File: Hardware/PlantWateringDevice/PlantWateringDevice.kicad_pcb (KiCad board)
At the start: 4 copper layers, 50 x 50 mm, 87 parts, among them J1 Conn_01x03_Pin, J3 Conn_01x03_Pin, J5 Conn_02x03_Odd_Even, J6 Barrel_Jack_Switch, M1 Motor_DC, Q1 AO3404A, SW1 SW_Push, SW6 SW_Push, SW7 SW_DIP_x02, SW8 SW_Push, U1 MCP6002-xSN, U10 74HC595, U2 L78L33_SO8, U3 PIC10F200-IOT, U4 74LVC1G3157, U5 74HC595, U9 74HC4052D

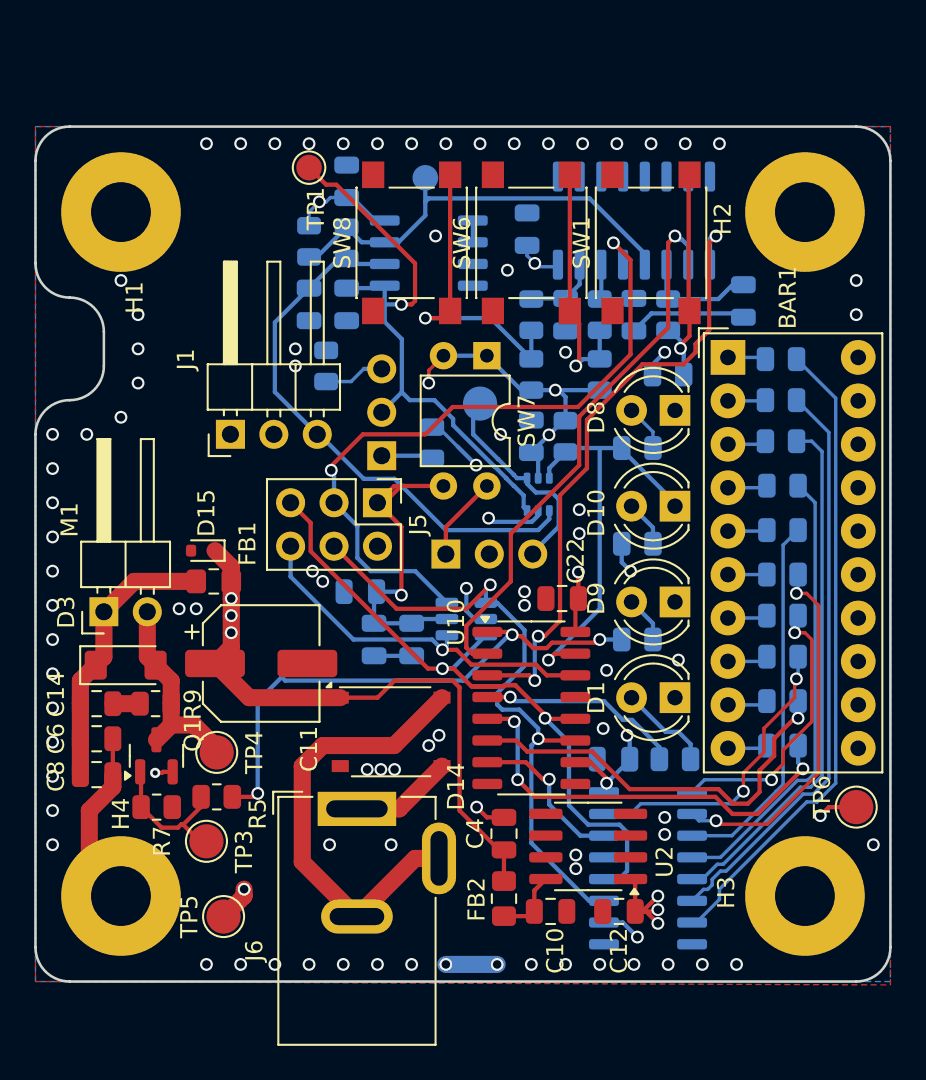
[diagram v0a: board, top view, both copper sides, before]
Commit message: circuit simplification
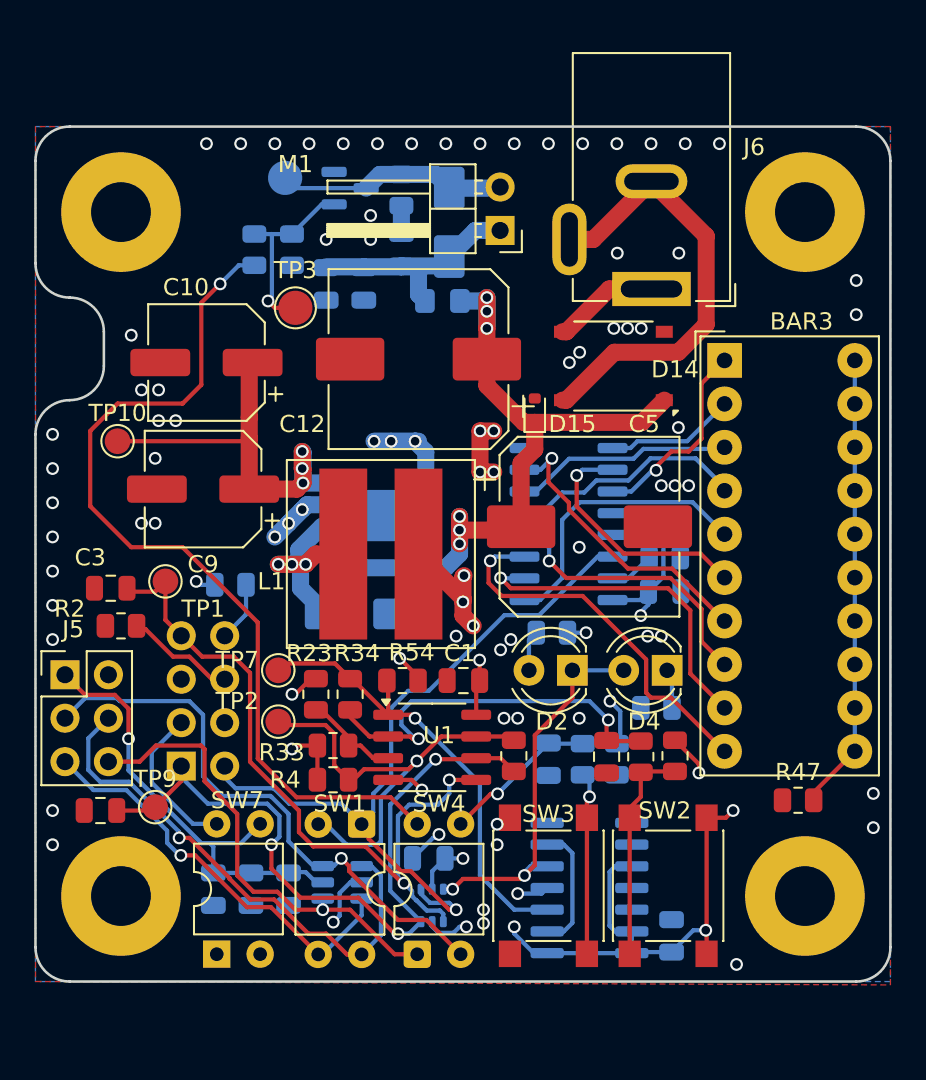
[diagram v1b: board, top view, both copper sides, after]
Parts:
- removed BAR1: HDSP-4830_2, Display:HDSP-4830
- removed C11: 100u/12v, Capacitor_SMD:CP_Elec_6.3x5.8
- removed C20, C22, C23, C24: 100n, Capacitor_SMD:C_0805_2012Metric
- removed D10, D8, D9: LED, LED_THT:LED_D4.0mm
- removed D3: D, Diode_SMD:D_MiniMELF
- removed FB2: FerriteBead, Inductor_SMD:L_0805_2012Metric_Pad1.15x1.40mm_HandSolder
- removed J3: Conn_01x03_Pin, Connector_PinHeader_2.54mm:PinHeader_1x03_P2.54mm_Vertical
- removed R10, R12, R13, R14, R15, R16, R17, R18, R19, R20, R21, R22: 220R, Resistor_SMD:R_0805_2012Metric
- removed R25, R27, R29: 10k, Resistor_SMD:R_0805_2012Metric
- removed R26, R28, R30: 100R, Resistor_SMD:R_0805_2012Metric
- removed RV1: 100k, Connector_PinHeader_2.54mm:PinHeader_1x03_P2.54mm_Vertical
- removed SW6, SW8: SW_Push, Button_Switch_SMD:SW_SPST_PTS645
- removed TP5, TP6, TP8: TestPoint, TestPoint:TestPoint_Pad_D2.0mm
- removed U10: 74HC595, Package_SO:SO-16_3.9x9.9mm_P1.27mm
- removed U4: 74LVC1G3157, Package_TO_SOT_SMD:SOT-363_SC-70-6
- removed U9: 74HC4052D, Package_SO:SO-16_3.9x9.9mm_P1.27mm
- added BAR3: HDSP-4830_2, Display:HDSP-4830, F.Cu at (175.3, 53.7)
- added C17: 100n, Capacitor_SMD:C_0805_2012Metric, B.Cu at (172.2, 87.3)
- added C21: 100n, Capacitor_SMD:C_0805_2012Metric, B.Cu at (171.8, 67.2)
- added C25: 100n, Capacitor_SMD:C_0805_2012Metric, B.Cu at (171.8, 63.2)
- added C7: 100n, Capacitor_SMD:C_0805_2012Metric, F.Cu at (168.4, 76.8)
- added D2: LED, LED_THT:LED_D4.0mm, F.Cu at (166.4, 71.8)
- added D4: LED, LED_THT:LED_D4.0mm, F.Cu at (171.9, 71.8)
- added D5: D_Schottky, Diode_SMD:D_SMA, B.Cu at (154.0, 68.5)
- added L1: 33u, PlantWateringDevice:SDR1006-330KL, F.Cu at (155.2, 65.0)
- added R11: 10k, Resistor_SMD:R_0805_2012Metric, F.Cu at (172.4, 76.8)
- added R24: 10k, Resistor_SMD:R_0805_2012Metric, F.Cu at (170.4, 76.8)
- added R31: 220R, Resistor_SMD:R_0805_2012Metric, B.Cu at (165.2, 69.6)
- added R32: 220R, Resistor_SMD:R_0805_2012Metric, B.Cu at (171.3, 74.0)
- added R33: 10k, Resistor_SMD:R_0805_2012Metric, F.Cu at (152.4, 76.2)
- added R34: 100k, Resistor_SMD:R_0805_2012Metric, F.Cu at (153.4, 73.2)
- added R47: 220R, Resistor_SMD:R_0805_2012Metric, F.Cu at (179.6, 79.4)
- added R53: 22k, Resistor_SMD:R_0805_2012Metric, B.Cu at (171.8, 65.2)
- added R54: 1k, Resistor_SMD:R_0805_2012Metric, F.Cu at (156.5, 72.4)
- added SW2: SW_Push, Button_Switch_SMD:SW_SPST_PTS645, F.Cu at (172.0, 84.4)
- added SW3: SW_Push, Button_Switch_SMD:SW_SPST_PTS645, F.Cu at (165.0, 84.4)
- added SW4: SW_DIP_x02, Package_DIP:DIP-4_W7.62mm, F.Cu at (157.3, 88.4)
- added TP10: TestPoint, TestPoint:TestPoint_Pad_D1.5mm, F.Cu at (139.8, 58.4)
- added TP7: TestPoint, TestPoint:TestPoint_Pad_D1.5mm, F.Cu at (149.2, 71.8)
- added TP9: TestPoint, TestPoint:TestPoint_Pad_D1.5mm, F.Cu at (142.0, 79.8)
- added U6: 74HC74, Package_SO:SO-14_3.9x8.65mm_P1.27mm, B.Cu at (167.4, 84.5)
- added U7: 4017, Package_SO:SO-16_3.9x9.9mm_P1.27mm, B.Cu at (166.2, 63.2)
- C1, C2, C3, R2, R3, R4, TP2, U1: moved to F.Cu
- C10: value 1u -> 220u; footprint Capacitor_SMD:C_0805_2012Metric -> Capacitor_SMD:CP_Elec_6.3x5.8
- C12: value 1u -> 680u/12v; footprint Capacitor_SMD:C_0805_2012Metric -> Capacitor_SMD:CP_Elec_10x10
- C14, C6, C8, FB1, Q1, R5, R7, R9, TP4: moved to B.Cu
- C4: value 1u -> 100n; moved to B.Cu
- C5: value 100n -> 680u/12v; footprint Capacitor_SMD:C_0805_2012Metric -> Capacitor_SMD:CP_Elec_10x10; moved to F.Cu
- C9: value 100n -> 220u; footprint Capacitor_SMD:C_0805_2012Metric -> Capacitor_SMD:CP_Elec_6.3x5.8; moved to F.Cu
- D1: value LED -> D_Schottky; footprint LED_THT:LED_D4.0mm -> Diode_SMD:D_SMA; moved to B.Cu
- J1: value Conn_01x03_Pin -> Conn_02x04_Counter_Clockwise; footprint Connector_PinHeader_2.54mm:PinHeader_1x03_P2.54mm_Horizontal -> Connector_PinHeader_2.54mm:PinHeader_2x04_P2.54mm_Vertical; moved to B.Cu
- R23: value 100k -> 10k; moved to F.Cu
- R6, R8: value 220R -> 10k
- SW1: value SW_Push -> SW_DIP_x02; footprint Button_Switch_SMD:SW_SPST_PTS645 -> Package_DIP:DIP-4_W7.62mm
- U2: value L78L33_SO8 -> 74LVC1G3157; footprint Package_SO:SOIC-8_3.9x4.9mm_P1.27mm -> Package_TO_SOT_SMD:SOT-363_SC-70-6; moved to B.Cu
- U5: value 74HC595 -> LM2596S-3.3; footprint Package_SO:SO-16_3.9x9.9mm_P1.27mm -> Package_SO:Infineon_PG-DSO-8-27_3.9x4.9mm_EP2.65x3mm
- moved SW7 38.4 mm to (145.6, 88.4), turned to 90 degrees
- moved SW1 38.0 mm to (154.1, 80.8), turned to -90 degrees
- moved C10 37.9 mm to (145.0, 53.8), turned to 180 degrees
- moved Q1 35.1 mm to (153.4, 43.6), turned to 0 degrees
- moved J6 34.9 mm to (171.0, 49.5), turned to 180 degrees
- moved C12 34.4 mm to (157.4, 53.6)
- moved TP4 33.8 mm to (149.6, 43.0), turned to 180 degrees
- moved R7 33.5 mm to (150.0, 47.2), turned to -90 degrees
- moved R9 33.3 mm to (156.4, 43.7), turned to 90 degrees
- moved TP2 32.9 mm to (149.2, 74.8), turned to 0 degrees
- moved C8 32.7 mm to (154.2, 49.2), turned to -90 degrees
- moved M1 32.2 mm to (162.2, 46.1), turned to 180 degrees
- moved R5 32.1 mm to (147.8, 47.2), turned to 90 degrees
- moved C2 32.0 mm to (138.8, 80.0), turned to 180 degrees
- moved C14 32.0 mm to (156.4, 47.2), turned to 90 degrees
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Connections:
- net DATA_IN renamed Net-(J5-Pin_3)
- net DATA_OUT renamed Net-(J5-Pin_6)
- C10 pad 1: Net-(U2-IN) -> +3V3
- C12 pad 1: +3V3 -> Net-(D14-+)
- C13 pad 1: +3V3 -> BUTTON
- C14 pad 1: Net-(D3-K) -> Net-(D1-K)
- C4 pad 1: +5V -> +3V3
- C5 pad 1: Net-(U9-X1) -> Net-(D14-+)
- C6 pad 1: Net-(D3-K) -> Net-(D1-K)
- C8 pad 1: Net-(D3-K) -> Net-(D1-K)
- C9 pad 1: Net-(U9-X2) -> +3V3
- D1 pad 1: GND -> Net-(D1-K)
- D14 pad 1: +5V -> Net-(D14-+)
- D15 pad 1: +5V -> Net-(D14-+)
- FB1 pad 1: +5V -> Net-(D14-+)
- FB1 pad 2: Net-(D3-K) -> Net-(D1-K)
- J1 pad 1: +3V3 -> HUMIDITY_SENSOR_IN
- J1 pad 2: GND -> DISPLAY_DATA
- J1 pad 3: HUMIDITY_SENSOR_IN -> DISPLAY_POWER
- J5 pad 4: CLK -> Net-(J5-Pin_4)
- J5 pad 5: STROBE -> Net-(J5-Pin_5)
- M1 pad 1: Net-(D3-K) -> Net-(D1-K)
- M1 pad 2: Net-(D3-A) -> Net-(D1-A)
- Q1 pad 3: Net-(D3-A) -> Net-(D1-A)
- R1 pad 1: Net-(R1-Pad1) -> POT_UP
- R2 pad 2: Net-(R2-Pad2) -> POT_DOWN
- R23 pad 1: /OutMUX/ENA_A_1 -> Net-(U1A-+)
- R23 pad 2: +3V3 -> GND
- R6 pad 1: Net-(D10-A) -> +3V3
- R6 pad 2: +3V3 -> Net-(R6-Pad2)
- R8 pad 1: Net-(BAR1-A-Pad10) -> Net-(R6-Pad2)
- R8 pad 2: Net-(U10-QF) -> BUTTON
- R9 pad 2: Net-(D3-A) -> Net-(D1-A)
- SW1 pad 1: GND -> DISPLAY_DATA
- SW1 pad 2: Net-(R29-Pad2) -> HUMIDITY_SENSOR_OUT
- TP4 pad 1: Net-(D3-A) -> Net-(D1-A)
- U1 pad 1: Net-(U1A--) -> Net-(U6A-C)
- U1 pad 3: GND -> Net-(U1A-+)
- U2 pad 1: +3V3 -> HUMIDITY_SENSOR_COMP
- U2 pad 3: GND -> HUMIDITY_SENSOR_IN
- U2 pad 4: unconnected-(U2-NC-Pad4) -> DISPLAY_DATA
- U2 pad 5: unconnected-(U2-NC-Pad5) -> +3V3
- U2 pad 6: GND -> Net-(D2-K)
- U3 pad 1: CLK -> Net-(J5-Pin_4)
- U3 pad 3: STROBE -> Net-(J5-Pin_5)
- U5 pad 1: Net-(U5-QB) -> Net-(D14-+)
- U5 pad 3: Net-(U5-QD) -> GND
- U5 pad 4: Net-(U5-QE) -> +3V3
- U5 pad 5: Net-(U5-QF) -> GND
- U5 pad 6: Net-(U5-QG) -> (no net)
- U5 pad 7: Net-(U5-QH) -> (no net)
- U5 pad 8: GND -> (no net)
- U5 pad 9: unconnected-(U5-QH&apos;-Pad9) -> (no net)
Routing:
- net DISPLAY_DATA: track 0.00 -> 43.1 mm, vias 0 -> 1
- net STROBE: track 42.5 -> 0.00 mm, vias 2 -> 0
- net Net-(D14-+): track 0.00 -> 42.1 mm, vias 0 -> 6
- net CLK: track 38.0 -> 0.00 mm, vias 2 -> 0
- net Net-(U5-QH): track 37.6 -> 0.00 mm
- net +5V: track 37.5 -> 0.00 mm, vias 4 -> 0
- net BUTTON_2: track 36.9 -> 0.00 mm, vias 3 -> 0
- net Net-(U5-QG): track 34.1 -> 0.00 mm
- net +3V3: track 53.1 -> 86.4 mm, vias 16 -> 18
- net BUTTON_1: track 32.6 -> 0.00 mm, vias 1 -> 0
- net Net-(U5-QF): track 30.8 -> 0.00 mm
- net Net-(J5-Pin_4): track 0.00 -> 30.6 mm, vias 0 -> 1
- net Net-(U5-QE): track 26.5 -> 0.00 mm
- net Net-(BAR3-K-Pad11): track 0.00 -> 26.3 mm
- net Net-(U6A-C): track 0.00 -> 25.7 mm, vias 0 -> 1
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- added copper zone on In1.Cu, net Net-(D14-+)
- removed copper zone on In1.Cu, net +5V

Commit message: model of 3d printed holder
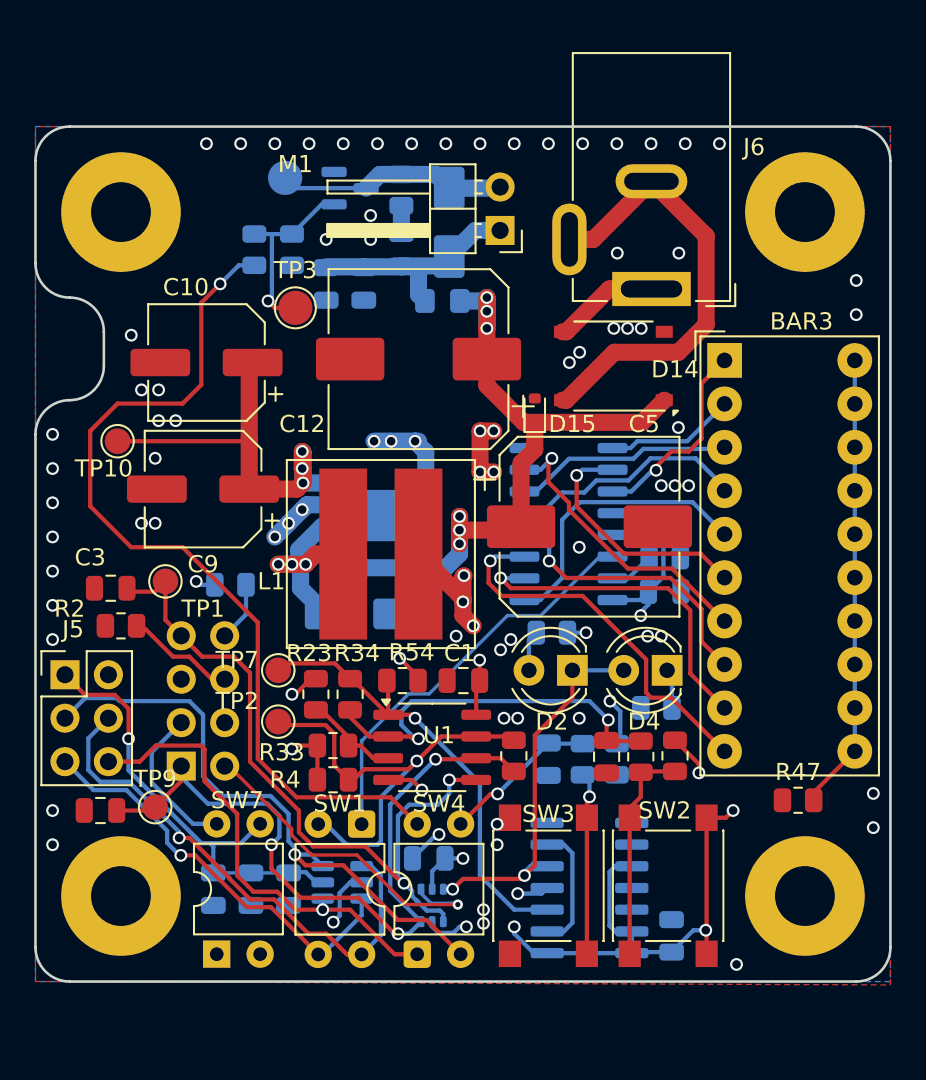
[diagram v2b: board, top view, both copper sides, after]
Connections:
- SW1 pad 1: DISPLAY_DATA -> DISPLAY_BARGRAPH
- U7 pad 14: DISPLAY_DATA -> DISPLAY_BARGRAPH
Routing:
- net DISPLAY_DATA: track 43.1 -> 19.6 mm
- net DISPLAY_BARGRAPH: track 0.00 -> 23.3 mm
- net Net-(J5-Pin_3): track 32.9 -> 35.0 mm

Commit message: improvements after eric's comments
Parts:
- removed C10, C9: 220u, Capacitor_SMD:CP_Elec_6.3x5.8
- removed D1, D5: D_Schottky, Diode_SMD:D_SMA
- removed D15: ESD5Zxx, Diode_SMD:D_SOD-523
- removed FB1: FerriteBead, Inductor_SMD:L_0805_2012Metric_Pad1.15x1.40mm_HandSolder
- removed L1: 33u, PlantWateringDevice:SDR1006-330KL
- removed U5: LM2596S-3.3, Package_SO:Infineon_PG-DSO-8-27_3.9x4.9mm_EP2.65x3mm
- TP4: moved to F.Cu
- moved TP4 15.0 mm to (164.6, 43.0), turned to 0 degrees
- moved TP3 2.06 mm to (149.2, 52.4)
- moved TP10 1.00 mm to (139.0, 59.0)
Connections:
- C1 pad 1: +3V3 -> VCC
- C12 pad 1: Net-(D14-+) -> VCC
- C14 pad 1: Net-(D1-K) -> VCC
- C17 pad 1: +3V3 -> VCC
- C21 pad 1: +3V3 -> VCC
- C25 pad 1: +3V3 -> VCC
- C4 pad 1: +3V3 -> VCC
- C5 pad 1: Net-(D14-+) -> VCC
- C6 pad 1: Net-(D1-K) -> VCC
- C8 pad 1: Net-(D1-K) -> VCC
- D14 pad 1: Net-(D14-+) -> VCC
- J1 pad 4: +3V3 -> VCC
- M1 pad 1: Net-(D1-K) -> VCC
- R1 pad 2: +3V3 -> VCC
- R31 pad 2: +3V3 -> VCC
- R33 pad 1: +3V3 -> VCC
- R4 pad 2: +3V3 -> VCC
- R54 pad 2: +3V3 -> VCC
- R6 pad 1: +3V3 -> VCC
- SW2 pad 2: +3V3 -> VCC
- SW7 pad 1: +3V3 -> VCC
- SW7 pad 2: +3V3 -> VCC
- TP10 pad 1: +3V3 -> VCC
- U1 pad 8: +3V3 -> VCC
- U2 pad 5: +3V3 -> VCC
- U6 pad 1: +3V3 -> VCC
- U6 pad 10: +3V3 -> VCC
- U6 pad 13: +3V3 -> VCC
- U6 pad 14: +3V3 -> VCC
- U6 pad 4: +3V3 -> VCC
- U7 pad 16: +3V3 -> VCC
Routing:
- net VCC: track 0.00 -> 99.8 mm, vias 0 -> 19
- net +3V3: track 86.4 -> 0.00 mm, vias 18 -> 0
- net Net-(D14-+): track 42.1 -> 0.00 mm, vias 6 -> 0
- net Net-(D1-K): track 14.2 -> 0.00 mm
- net Net-(D5-K): track 12.5 -> 0.00 mm, vias 3 -> 0
- net PUMP_ON_OFF: track 52.3 -> 40.5 mm
- net GND: track 28.2 -> 18.6 mm, vias 81 -> 68
- net Net-(M1--): track 12.6 -> 10.3 mm
- added copper zone on In1.Cu, net VCC
- removed copper zone on In1.Cu, net +3V3
- removed copper zone on In1.Cu, net Net-(D14-+)

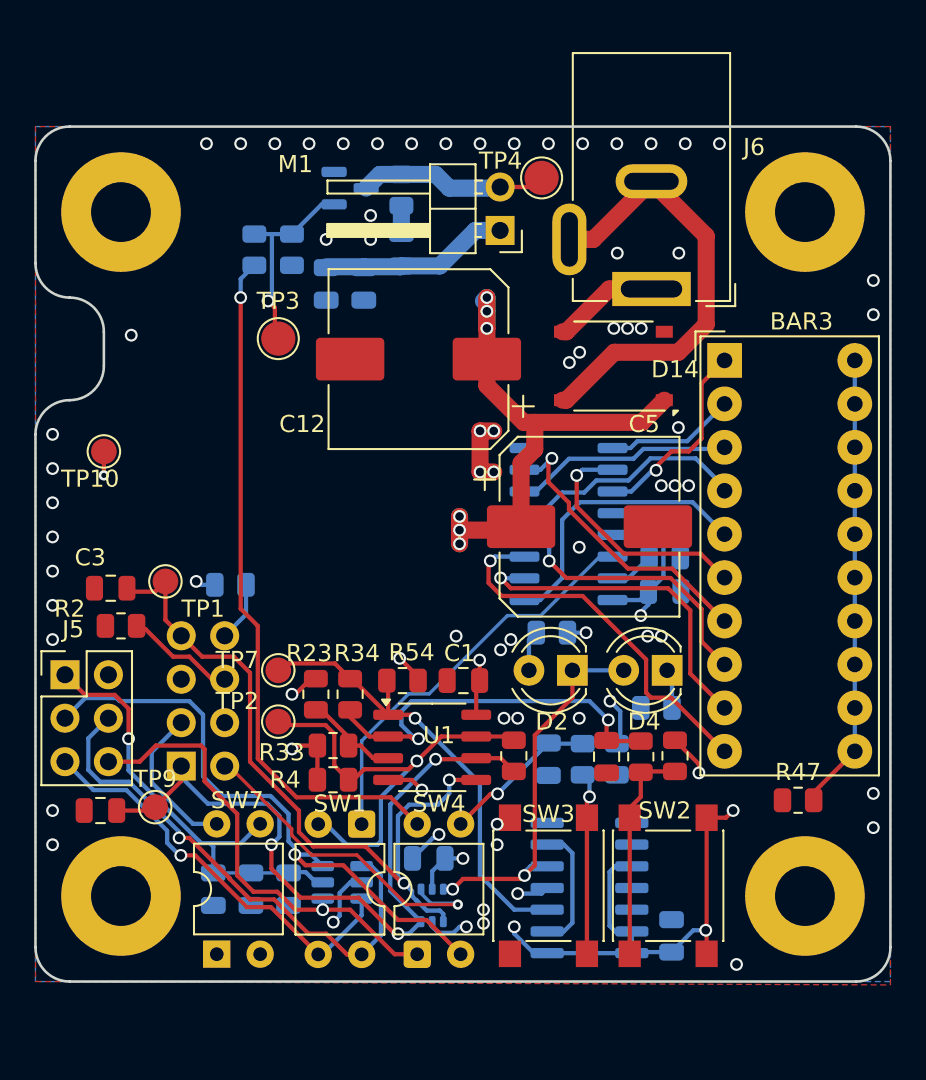
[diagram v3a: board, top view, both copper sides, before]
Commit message: fixes before sending pcb and 3d model to production
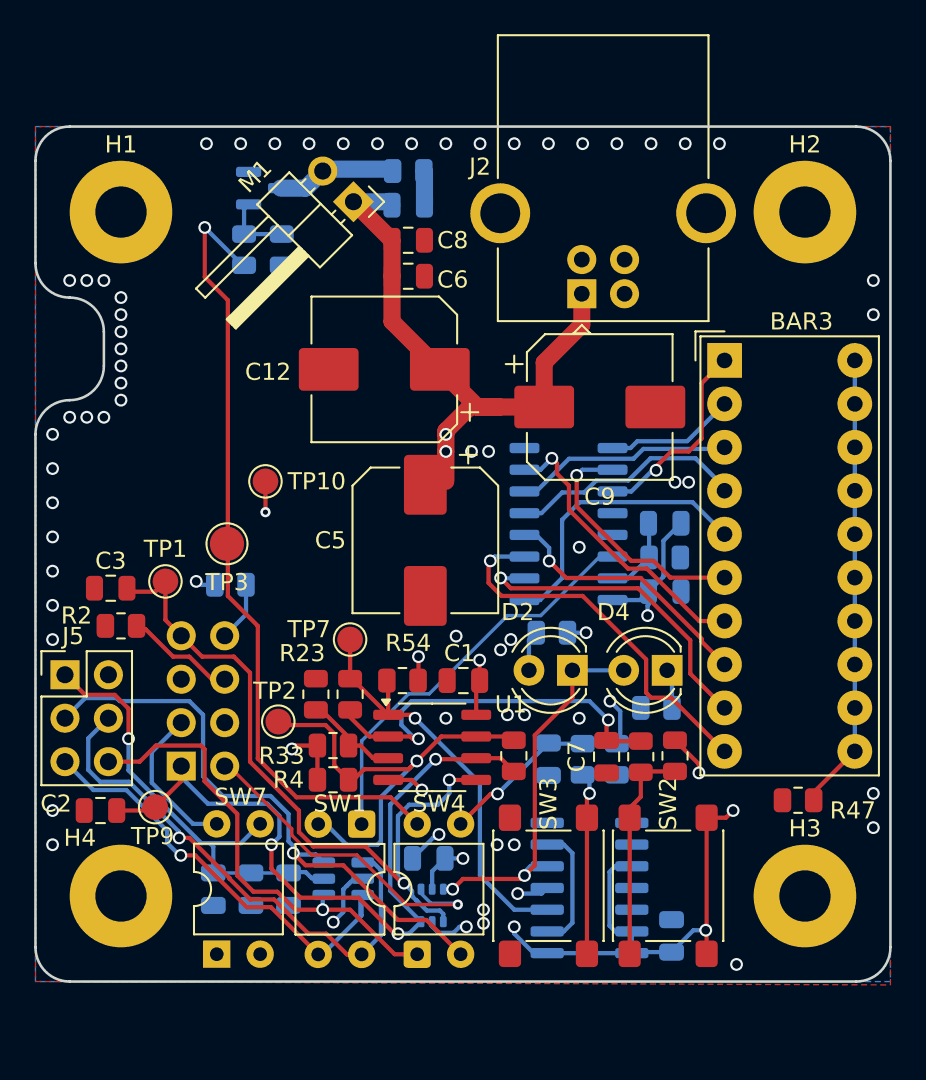
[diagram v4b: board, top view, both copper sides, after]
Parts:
- removed D14: ABS2, Diode_SMD:Diode_Bridge_Diotec_ABS
- removed J6: Barrel_Jack_Switch, Connector_BarrelJack:BarrelJack_GCT_DCJ200-10-A_Horizontal
- removed TP4: TestPoint, TestPoint:TestPoint_Pad_D2.0mm
- removed U3: PIC10F200-IOT, Package_TO_SOT_SMD:SOT-23-6
- added C9: 470u/16v, Capacitor_SMD:CP_Elec_8x10, F.Cu at (168.0, 56.4)
- added J2: USB_B, Connector_USB:USB_B_OST_USB-B1HSxx_Horizontal, F.Cu at (166.9, 49.8)
- added U4: PIC10F202-IOT, Package_TO_SOT_SMD:SOT-23-6, B.Cu at (153.0, 84.0)
- C12, C5: value 680u/12v -> 470u/16v; footprint Capacitor_SMD:CP_Elec_10x10 -> Capacitor_SMD:CP_Elec_8x10
- C6, C8: moved to F.Cu
- H1, H2, H3, H4: footprint MountingHole:MountingHole_3.5mm_Pad -> MountingHole:MountingHole_3mm_Pad
- SW2, SW3: footprint Button_Switch_SMD:SW_SPST_PTS645 -> Button_Switch_SMD:SW_SPST_PTS645Sx43SMTR92
- U7: value 4017 -> 74HC4017D
- moved TP3 12.4 mm to (146.2, 64.4)
- moved C5 9.63 mm to (157.8, 64.2), turned to -90 degrees
- moved TP10 9.61 mm to (148.4, 60.8)
- moved M1 8.74 mm to (153.6, 44.4), turned to -135 degrees
- moved Q1 5.00 mm to (148.4, 43.6)
- moved C6 4.82 mm to (156.8, 48.8), turned to 0 degrees
- moved TP7 4.57 mm to (153.4, 70.0)
- moved C8 3.64 mm to (156.8, 46.6), turned to 0 degrees
- moved C14 2.63 mm to (156.8, 44.6), turned to 0 degrees
- moved C12 2.09 mm to (155.4, 54.2)
- moved R9 1.18 mm to (156.8, 42.6), turned to 180 degrees
- moved R5 0.60 mm to (147.2, 47.2)
- moved R7 0.60 mm to (149.4, 47.2)
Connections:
- TP3 pad 1: Net-(Q1-G) -> PUMP_ON_OFF
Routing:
- net Net-(D14-Pad4): track 26.1 -> 0.00 mm
- net Net-(Q1-G): track 11.6 -> 4.05 mm, vias 1 -> 0
- net Net-(D14-Pad3): track 6.24 -> 0.00 mm
- net PUMP_ON_OFF: track 40.5 -> 46.4 mm
- net VCC: track 99.8 -> 94.2 mm, vias 19 -> 15
- net GND: track 18.6 -> 13.0 mm, vias 68 -> 64
- net Net-(M1--): track 10.3 -> 6.90 mm
- net Net-(U6A-C): track 25.7 -> 23.8 mm
- net Net-(J5-Pin_5): track 24.1 -> 25.2 mm
- net Net-(U7-Q1): track 19.8 -> 18.8 mm
- net Net-(U7-Q2): track 15.7 -> 14.7 mm

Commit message: fix #29, fix #31
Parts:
- removed R3: 470k, Resistor_SMD:R_0805_2012Metric
- R31, R32: value 220R -> 510R
- R47: value 220R -> 120R
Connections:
- net DISPLAY_DATA renamed LCD_DATA
- net HUMIDITY_SENSOR_COMP renamed POTENTIOMETER_DATA
- net HUMIDITY_SENSOR_IN renamed HUMIDITY_SENSOR
- net HUMIDITY_SENSOR_OUT renamed HUMIDITY_COMPARATION
- net POT_DOWN renamed POTENTIOMETER_VSS
- net POT_UP renamed POTENTIOMETER_VCC
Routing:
- net HUMIDITY_SENSOR: track 41.8 -> 39.3 mm
- net HUMIDITY_COMPARATION: track 25.6 -> 23.6 mm
